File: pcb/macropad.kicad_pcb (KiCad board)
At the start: 2 copper layers, 66 x 99.8 mm, 26 parts, among them J1 0.91 OLED display, SW1 SW_Push, SW10 SW_Push, SW11 SW_Push, SW12 SW_Push, SW2 SW_Push, SW3 SW_Push, SW4 SW_Push, SW5 SW_Push, SW6 SW_Push, SW7 SW_Push, SW8 SW_Push, SW9 SW_Push, U1 MOUDLE-SEEEDUINO-XIAO

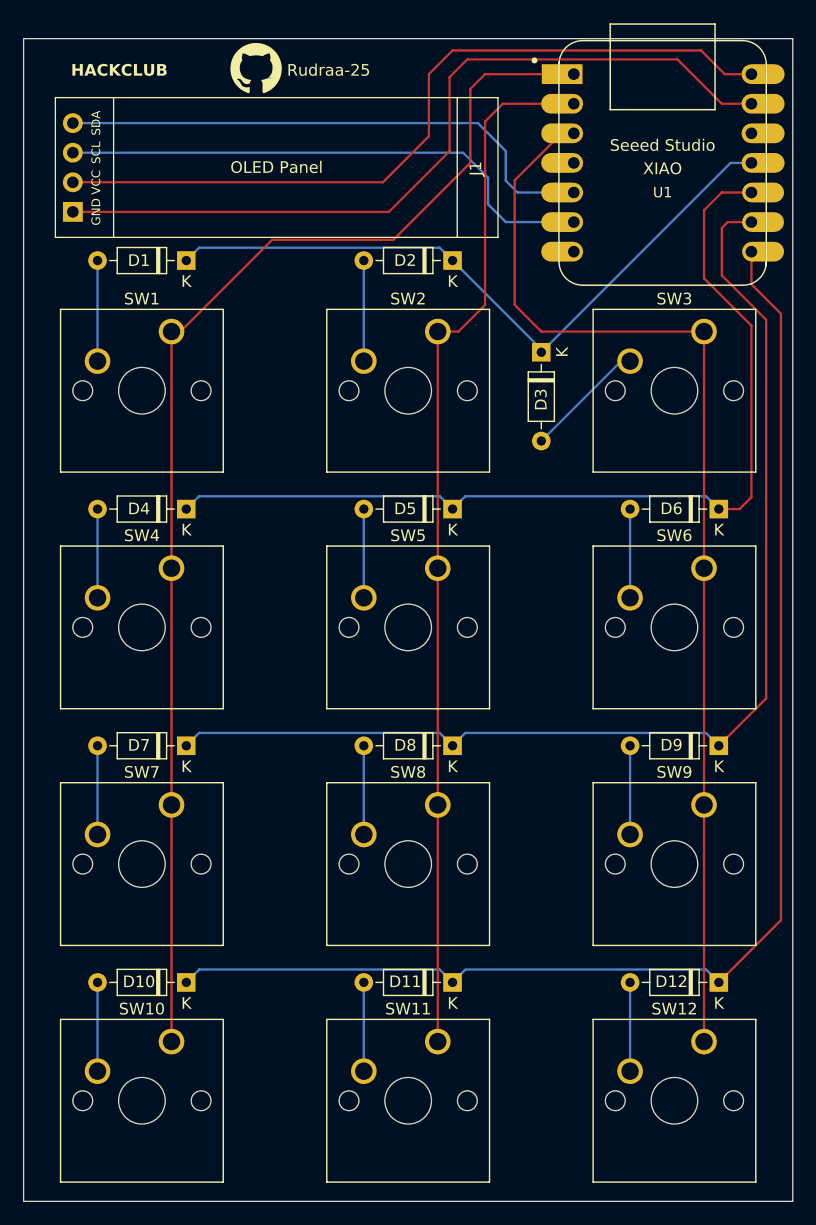
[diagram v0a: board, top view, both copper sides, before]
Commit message: Initial commit of cherryblossom pad for Hackpad
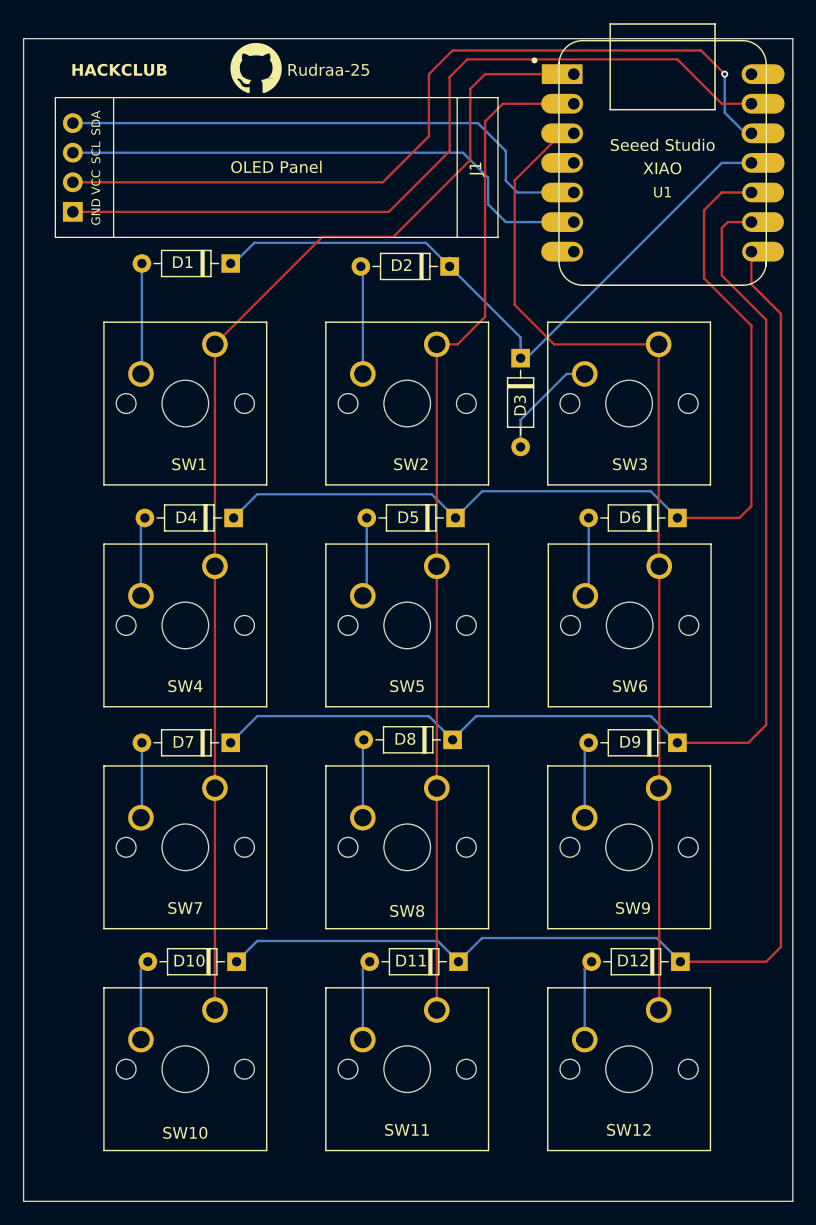
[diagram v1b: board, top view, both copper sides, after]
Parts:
- moved SW12 4.74 mm to (166.3, 129.1)
- moved D10 4.67 mm to (130.0, 125.0)
- moved SW10 4.61 mm to (128.2, 129.1)
- moved SW9 4.15 mm to (166.3, 110.1)
- moved D4 4.13 mm to (129.8, 86.9)
- moved SW3 4.05 mm to (166.3, 72.0)
- moved SW7 3.99 mm to (128.2, 110.1)
- moved SW1 3.88 mm to (128.2, 72.0)
- moved SW6 3.85 mm to (166.3, 91.0)
- moved D1 3.82 mm to (129.5, 65.0)
- moved D7 3.82 mm to (129.5, 106.2)
- moved D12 3.75 mm to (168.1, 125.0)
- moved SW4 3.73 mm to (128.2, 91.0)
- moved D6 3.64 mm to (167.9, 86.9)
- moved D9 3.57 mm to (167.9, 106.2)
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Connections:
- U1 pad 12: unconnected-(U1-3V3-Pad12) -> VCC
- U1 pad 14: VCC -> unconnected-(U1-5V-Pad14)
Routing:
- net Net-(U1-PA02_A0_D0): track 108.5 -> 101.2 mm
- net Net-(U1-PA10_A2_D2): track 95.5 -> 88.3 mm
- net VCC: track 67.0 -> 71.0 mm, vias 0 -> 1
- net Net-(U1-PA4_A1_D1): track 90.1 -> 87.4 mm
- net Net-(D10-K): track 113.3 -> 110.9 mm
- net Net-(D4-K): track 81.9 -> 80.3 mm
- net Net-(D3-A): track 10.8 -> 9.46 mm
- net Net-(D7-A): track 7.62 -> 6.47 mm
- net Net-(D1-K): track 60.3 -> 59.3 mm
- net Net-(D7-K): track 98.1 -> 97.3 mm
- net Net-(D6-A): track 7.62 -> 6.81 mm
- net Net-(D5-A): track 7.62 -> 6.83 mm
- net Net-(D4-A): track 7.62 -> 6.83 mm
- net Net-(D8-A): track 7.62 -> 6.84 mm
- net Net-(D2-A): track 8.64 -> 9.30 mm
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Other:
- board text added: "D1"
- board text added: "D2"
